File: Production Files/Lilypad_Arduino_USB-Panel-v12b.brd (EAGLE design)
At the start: 125.7 x 125.7 mm, 187 parts, among them U1 MCP73831, U10 MCP73831, U11 MIC5219, U13 ATMEGA32U41:1-LESS_PASTE, U14 MCP73831, U15 MIC5219, U2 MIC5219, U3 ATMEGA32U41:1-LESS_PASTE, U4 ATMEGA32U41:1-LESS_PASTE, U6 MCP73831, U7 MIC5219, U9 ATMEGA32U41:1-LESS_PASTE, Y1 8MHz, Y2 8MHz, Y3 8MHz, Y4 8MHz

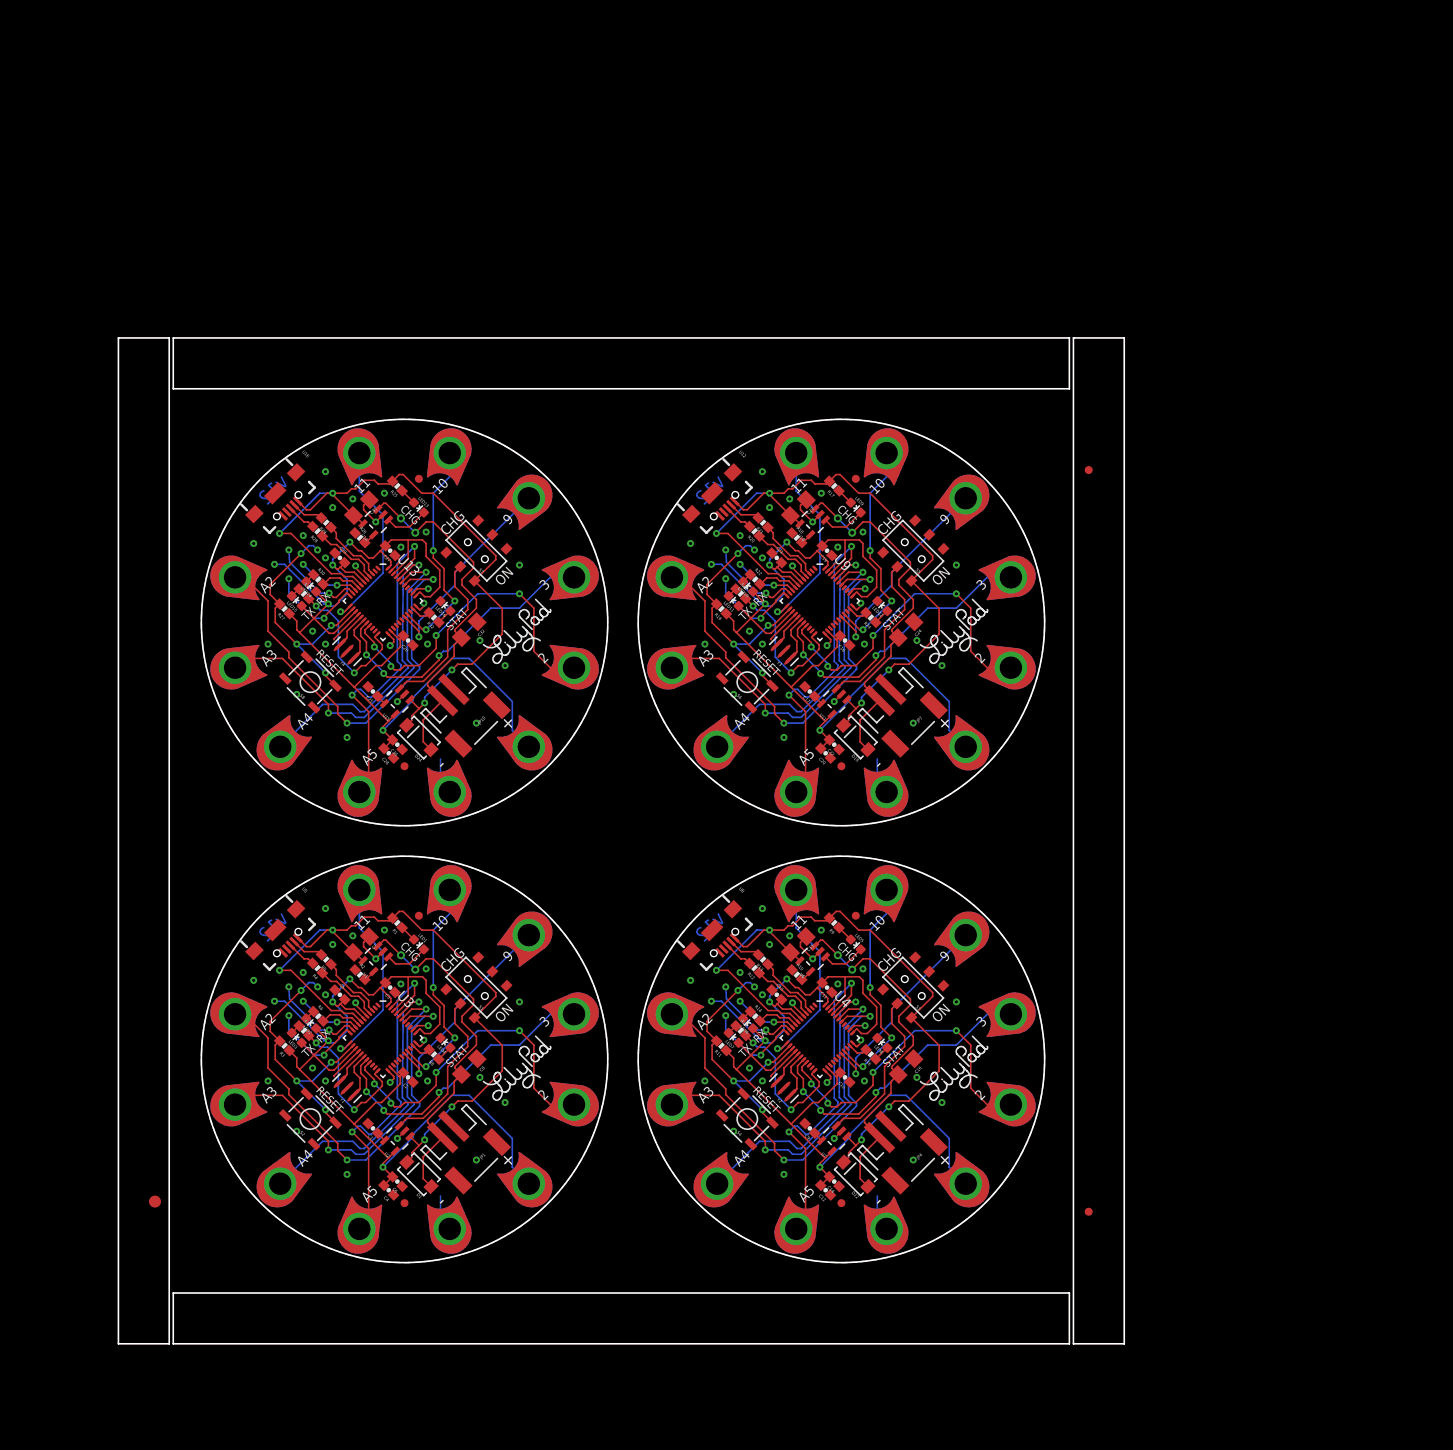
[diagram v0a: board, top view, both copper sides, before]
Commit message: New production panel v12b - strength tabs and v-scores
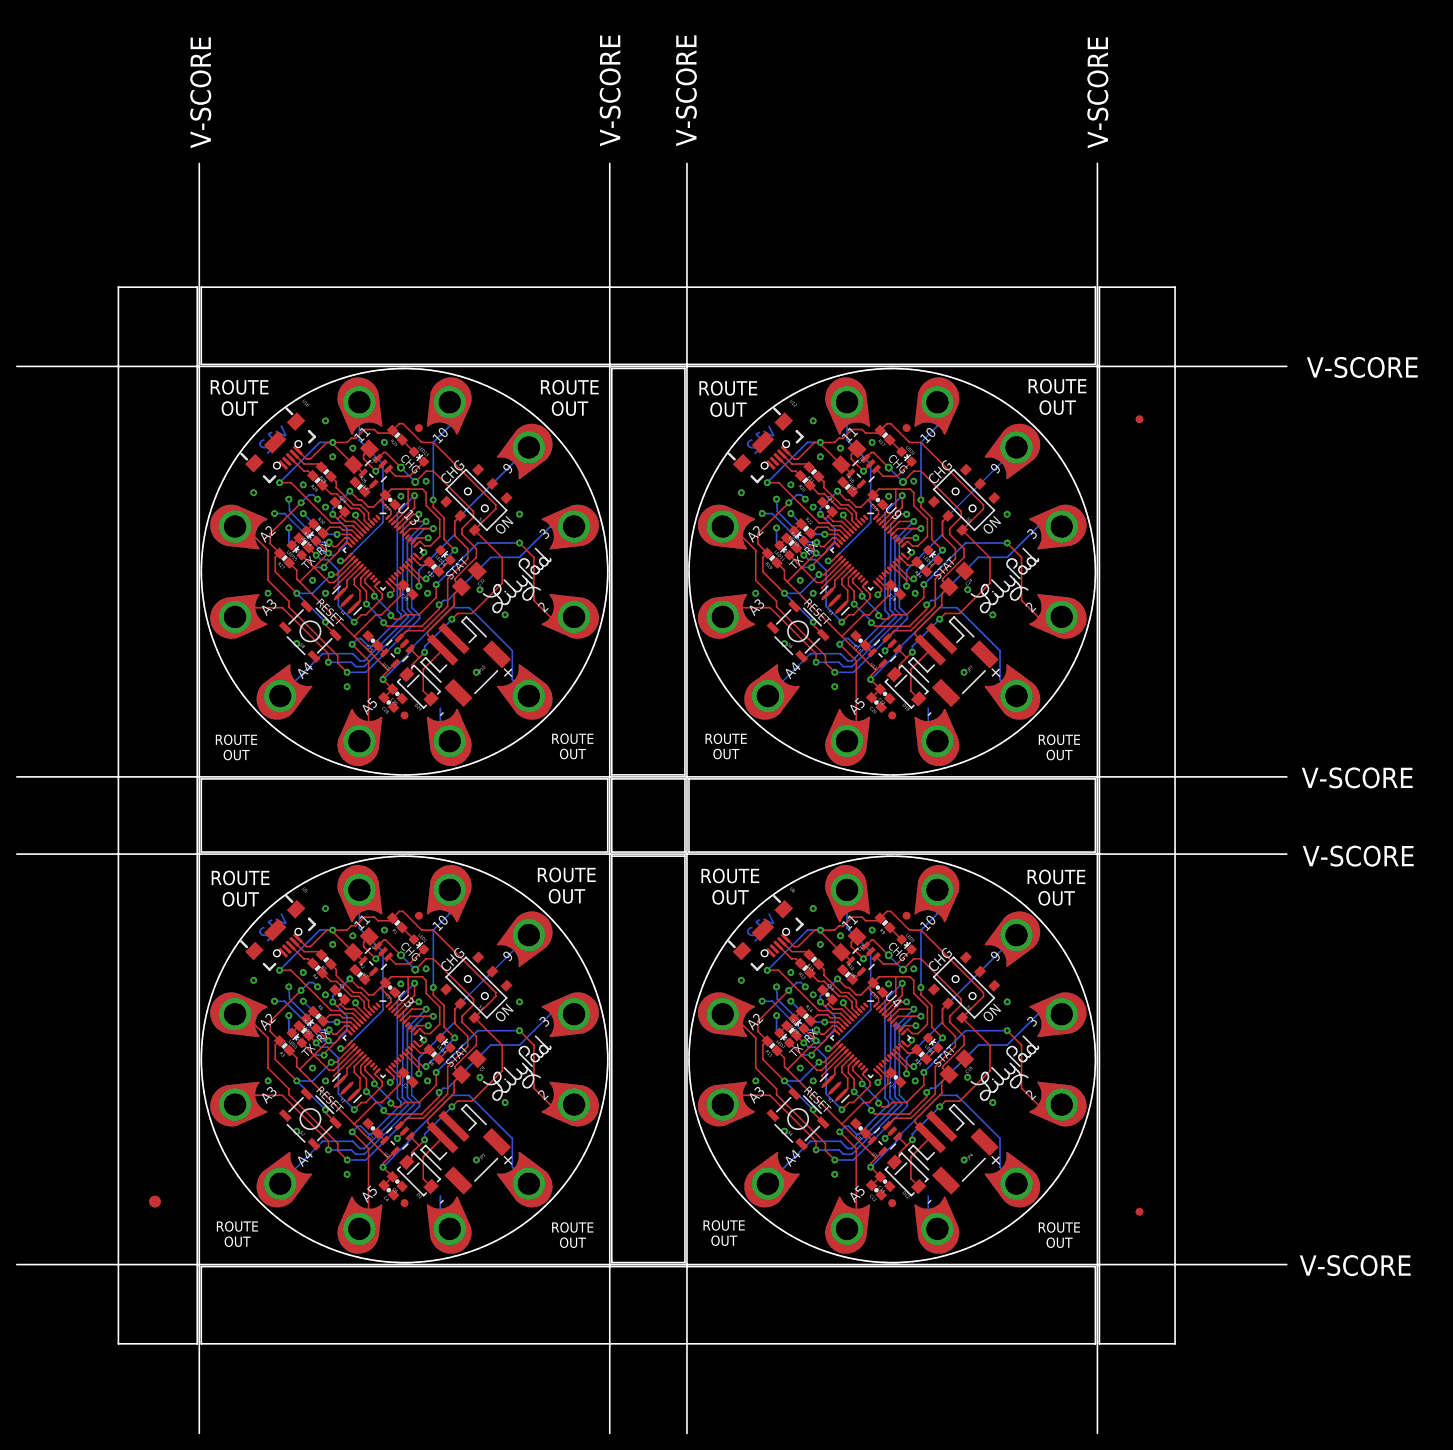
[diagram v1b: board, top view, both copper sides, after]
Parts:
- moved C17 8.98 mm to (92.8, 87.9)
- moved D17 8.98 mm to (91.1, 117.7)
- moved R22 8.98 mm to (86.0, 101.9)
- moved U$11 8.98 mm to (98.9, 101.5)
- moved U$9 8.98 mm to (96.7, 96.5)
- moved A10 8.98 mm to (75.5, 90.9)
- moved A11 8.98 mm to (91.1, 75.3)
- moved C19 8.98 mm to (94.9, 105.5)
- moved C20 8.98 mm to (94.8, 80.2)
- moved C21 8.98 mm to (88.6, 104.6)
- moved C22 8.98 mm to (95.8, 81.2)
- moved C24 8.98 mm to (104.8, 95.6)
- moved D13 8.98 mm to (117.9, 90.9)
- moved D16 8.98 mm to (102.4, 117.7)
- moved E$5 8.98 mm to (127.6, 115.6)
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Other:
- board size 125.7 x 125.7 mm -> 158.8 x 158.8 mm
- board text added: "ROUTE OUT"
- board text added: "V-SCORE"
